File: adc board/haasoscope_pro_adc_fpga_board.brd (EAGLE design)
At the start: 220 x 160 mm, 558 parts, among them CN2 12Vin, IC1 ADC12DL2500ACF, IC13 LMH5401IRMST, IC14 LMH6401IRMZR, IC15 SN74AVC4T774PWR, IC17 DAC8562SDGSR, IC18 TLV9102IPWR, IC2 SN74AVC4T774PWR, IC21 LMH5401IRMST, IC22 TPS7A7200RGTR, IC23 TPS7A7200RGTR, IC24 TPS7A7200RGTR, IC25 TPS72325DBVR, IC26 TPS7A7200RGTR, IC27 TPS7A7200RGTR, IC28 TPS7A7200RGTR, IC29 LMH6401IRMZR, IC3 ADC102S021CIMM_NOPB, IC30 SN74AVC4T774PWR, IC33 TLV9102IPWR, IC4 TLV9102IPWR, IC5 EP4CE30F23C6N, IC6 EPCQ16ASI8N, IC8 FT232HQ, IC9 93LC56B, J10 8pin, J11 8pin, J13 8pin, J14 2x5, J15 test1, J2 test1, J30 2p-2.54, J31 2p-2.54, J32 2p-2.54, J33 2p-2.54, J34 2p-2.54, J35 2p-2.54, J36 2p-2.54, J37 2p-2.54, J39 2p-2.54, J40 2p-2.54, J41 2p-2.54, J42 2p-2.54, J43 2p-2.54, J44 2p-2.54, J45 2p-2.54, J46 2p-2.54, J8 8pin, K10 G6K-2F-RF-DC3, K11 G6K-2F-RF-DC3, K12 G6K-2F-RF-DC3, K5 AQY21SOP, K6 G6K-2F-RF-DC3, K7 G6K-2F-RF-DC3, K9 AQY21SOP, Q4 S8050, Q5 S8050, Q7 S8050, Q8 S8050, Q9 S8050, SW3 SKQGADE010, SW4 SKQGADE010, U2 ADF4350BCPZ, U6 AMS1117-1.2, X1 USBC, Y2 OSCILLATORSMD-5X3, Y3 12MHz

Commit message: minor vias etc
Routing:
- net 2V5-: track 126.2 -> 131.7 mm, vias 22 -> 24
- net 2V5+: track 147.5 -> 152.9 mm, vias 23 -> 25
- net AMPSCLK: track 17.7 -> 22.2 mm
- net AMPSCS: track 17.8 -> 19.7 mm
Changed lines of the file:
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@@
 <wire x1="69.5" y1="41.5" x2="69.9" y2="41.5" width="0.1524" layer="1"/>
 <wire x1="69.9" y1="41.5" x2="70.4" y2="41" width="0.1524" layer="1"/>
-<wire x1="70.4" y1="41" x2="71" y2="41" width="0.1524" layer="1"/>
-<wire x1="71" y1="41" x2="71.2" y2="40.8" width="0.1524" layer="1"/>
+<wire x1="70.4" y1="41" x2="70.56" y2="41" width="0.1524" layer="1"/>
+<wire x1="70.76" y1="40.8" x2="71.2" y2="40.8" width="0.1524" layer="1"/>
+<wire x1="70.76" y1="40.8" x2="70.56" y2="41" width="0.1524" layer="1"/>
 <wire x1="71.2" y1="40.8" x2="72.2390125" y2="40.8" width="0.1524" layer="1"/>
 <wire x1="72.531" y1="40.881" x2="72.65" y2="41" width="0.1524" layer="1"/>
@@
 <wire x1="47.5" y1="115" x2="47.562" y2="115.025" width="0.1524" layer="1"/>
 <wire x1="87" y1="49" x2="86" y2="49" width="0.1524" layer="1"/>
+<via x="70.5" y="103" extent="1-16" drill="0.35"/>
+<wire x1="71.85" y1="102.75" x2="71.49" y2="102.75" width="0.2" layer="1"/>
+<wire x1="71.49" y1="102.75" x2="71.23" y2="103.01" width="0.2" layer="1"/>
+<wire x1="71.23" y1="103.01" x2="70.51" y2="103.01" width="0.2" layer="1"/>
+<wire x1="70.51" y1="103.01" x2="70.5" y2="103" width="0.2" layer="1"/>
+<wire x1="70.5" y1="103" x2="69.546025" y2="103" width="0.2" layer="1"/>
+<wire x1="69.546025" y1="103" x2="69.444025" y2="102.898" width="0.2" layer="1"/>
+<wire x1="69.444025" y1="102.898" x2="69.198" y2="102.898" width="0.2" layer="1"/>
+<wire x1="69.198" y1="102.898" x2="69.05" y2="102.75" width="0.2" layer="1"/>
+<via x="70.78" y="115.7" extent="1-16" drill="0.35"/>
+<wire x1="70.58" y1="115.5" x2="70.78" y2="115.7" width="0.1524" layer="1"/>
+<wire x1="69.35" y1="115.5" x2="70.58" y2="115.5" width="0.1524" layer="1"/>
+<wire x1="71.6" y1="115.5" x2="70.98" y2="115.5" width="0.1524" layer="1"/>
+<wire x1="70.98" y1="115.5" x2="70.78" y2="115.7" width="0.1524" layer="1"/>
 </signal>
 <signal name="2V5-" class="1">
@@
 <wire x1="70.029" y1="52.129" x2="70.15" y2="52.25" width="0.1524" layer="1"/>
 <wire x1="70.15" y1="52.25" x2="70.4657875" y2="52.25" width="0.1524" layer="1"/>
-<wire x1="70.4657875" y1="52.25" x2="70.5697875" y2="52.354" width="0.1524" layer="1"/>
-<wire x1="71.454" y1="52.354" x2="71.5" y2="52.4" width="0.1524" layer="1"/>
-<wire x1="70.5697875" y1="52.354" x2="71.454" y2="52.354" width="0.1524" layer="1"/>
+<wire x1="70.4657875" y1="52.25" x2="70.6197875" y2="52.404" width="0.1524" layer="1"/>
+<wire x1="71.5" y1="52.4" x2="71.496" y2="52.404" width="0.1524" layer="1"/>
+<wire x1="71.496" y1="52.404" x2="70.6197875" y2="52.404" width="0.1524" layer="1"/>
 <wire x1="71.5" y1="52.4" x2="72.5157875" y2="52.4" width="0.1524" layer="1"/>
 <wire x1="72.831" y1="52.369" x2="72.95" y2="52.25" width="0.1524" layer="1"/>
@@
 <wire x1="20.5" y1="123.625" x2="20.5" y2="123.7" width="0.1524" layer="1"/>
 <wire x1="51.5" y1="119" x2="52.95" y2="119" width="0.1524" layer="1"/>
+<via x="70.5" y="104" extent="1-16" drill="0.35"/>
+<wire x1="69.05" y1="104.25" x2="69.38" y2="104.25" width="0.2" layer="1"/>
+<wire x1="69.63" y1="104" x2="70.5" y2="104" width="0.2" layer="1"/>
+<wire x1="69.63" y1="104" x2="69.38" y2="104.25" width="0.2" layer="1"/>
+<wire x1="70.5" y1="104" x2="71.353975" y2="104" width="0.2" layer="1"/>
+<wire x1="71.353975" y1="104" x2="71.455975" y2="104.102" width="0.2" layer="1"/>
+<wire x1="71.455975" y1="104.102" x2="71.702" y2="104.102" width="0.2" layer="1"/>
+<wire x1="71.702" y1="104.102" x2="71.85" y2="104.25" width="0.2" layer="1"/>
+<via x="70.15" y="116.34" extent="1-16" drill="0.35"/>
+<wire x1="69.35" y1="116.5" x2="69.51" y2="116.34" width="0.1524" layer="1"/>
+<wire x1="70.15" y1="116.34" x2="69.51" y2="116.34" width="0.1524" layer="1"/>
+<wire x1="71.65" y1="116.5" x2="71.49" y2="116.34" width="0.1524" layer="1"/>
+<wire x1="71.49" y1="116.34" x2="70.15" y2="116.34" width="0.1524" layer="1"/>
 </signal>
 <signal name="SCS3_IN1">
@@
 <wire x1="85.5" y1="53" x2="85.5" y2="51.087" width="0.1524" layer="1"/>
 <wire x1="85.5" y1="51.087" x2="85.475" y2="51.062" width="0.1524" layer="1"/>
-<wire x1="70.75" y1="53.25" x2="70.15" y2="53.25" width="0.0889" layer="1"/>
-<wire x1="70.875" y1="53.125" x2="70.75" y2="53.25" width="0.0889" layer="1"/>
-<wire x1="71.875" y1="53.125" x2="70.875" y2="53.125" width="0.0889" layer="3"/>
-<wire x1="72.25" y1="53.5" x2="71.875" y2="53.125" width="0.0889" layer="3"/>
-<wire x1="85" y1="53.5" x2="72.25" y2="53.5" width="0.0889" layer="3"/>
+<wire x1="85" y1="53.5" x2="73.5" y2="53.5" width="0.0889" layer="3"/>
 <wire x1="85.5" y1="53" x2="85" y2="53.5" width="0.0889" layer="3"/>
-<via x="70.875" y="53.125" extent="1-16" drill="0.2"/>
+<via x="68" y="53" extent="1-16" drill="0.35"/>
+<wire x1="69.31493125" y1="53.21645" x2="68.94506875" y2="53.21645" width="0.0889" layer="3"/>
+<wire x1="68.94506875" y1="53.21645" x2="68.72861875" y2="53" width="0.0889" layer="3"/>
+<wire x1="68.72861875" y1="53" x2="68" y2="53" width="0.0889" layer="3"/>
+<wire x1="73.5" y1="53.5" x2="73.15355" y2="53.15355" width="0.0889" layer="3"/>
+<wire x1="73.15355" y1="53.15355" x2="69.37783125" y2="53.15355" width="0.0889" layer="3"/>
+<wire x1="69.37783125" y1="53.15355" x2="69.31493125" y2="53.21645" width="0.0889" layer="3"/>
+<wire x1="68" y1="53" x2="68.25" y2="53.25" width="0.0889" layer="1"/>
+<wire x1="68.25" y1="53.25" x2="70.15" y2="53.25" width="0.0889" layer="1"/>
 </signal>
 <signal name="AMPSCS">
@@
 <wire x1="84.875" y1="51" x2="84.825" y2="51.062" width="0.1524" layer="1"/>
 <via x="85.125" y="49.75" extent="1-16" drill="0.3048"/>
-<wire x1="71.125" y1="52.75" x2="70.15" y2="52.75" width="0.0889" layer="1"/>
-<wire x1="71.25" y1="52.875" x2="71.125" y2="52.75" width="0.0889" layer="1"/>
-<wire x1="72.25" y1="52.875" x2="71.25" y2="52.875" width="0.0889" layer="1"/>
-<wire x1="74.875" y1="50.25" x2="72.25" y2="52.875" width="0.0889" layer="3"/>
-<wire x1="84.625" y1="50.25" x2="74.875" y2="50.25" width="0.0889" layer="3"/>
 <wire x1="85.125" y1="49.75" x2="84.625" y2="50.25" width="0.0889" layer="3"/>
-<via x="72.25" y="52.875" extent="1-16" drill="0.2"/>
+<wire x1="71.65" y1="50.25" x2="69.13" y2="52.77" width="0.0889" layer="3"/>
+<via x="69.13" y="52.77" extent="1-16" drill="0.35"/>
+<wire x1="69.13" y1="52.77" x2="70.13" y2="52.77" width="0.0889" layer="1"/>
+<wire x1="70.13" y1="52.77" x2="70.15" y2="52.75" width="0.0889" layer="1"/>
+<wire x1="84.625" y1="50.25" x2="71.65" y2="50.25" width="0.0889" layer="3"/>
 </signal>
 <signal name="AOFFSET">

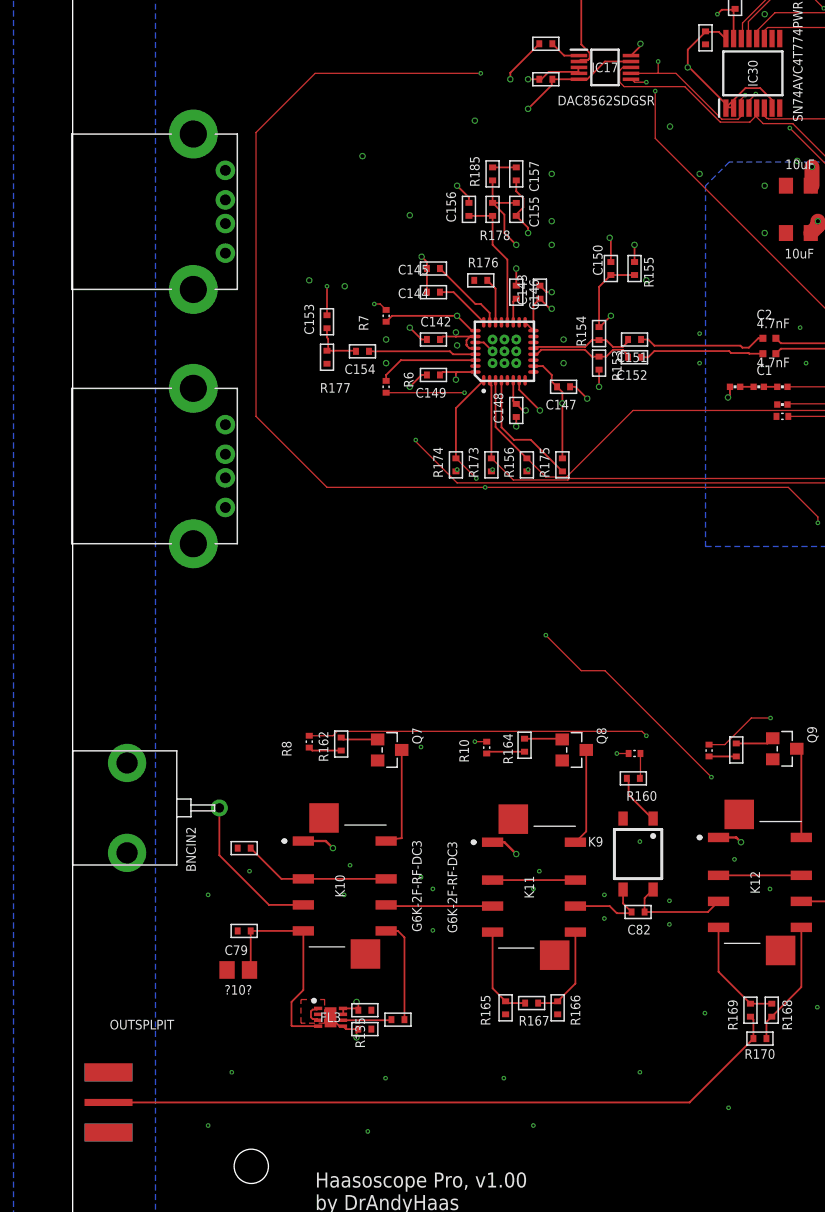
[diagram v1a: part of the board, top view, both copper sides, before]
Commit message: move connectors a little
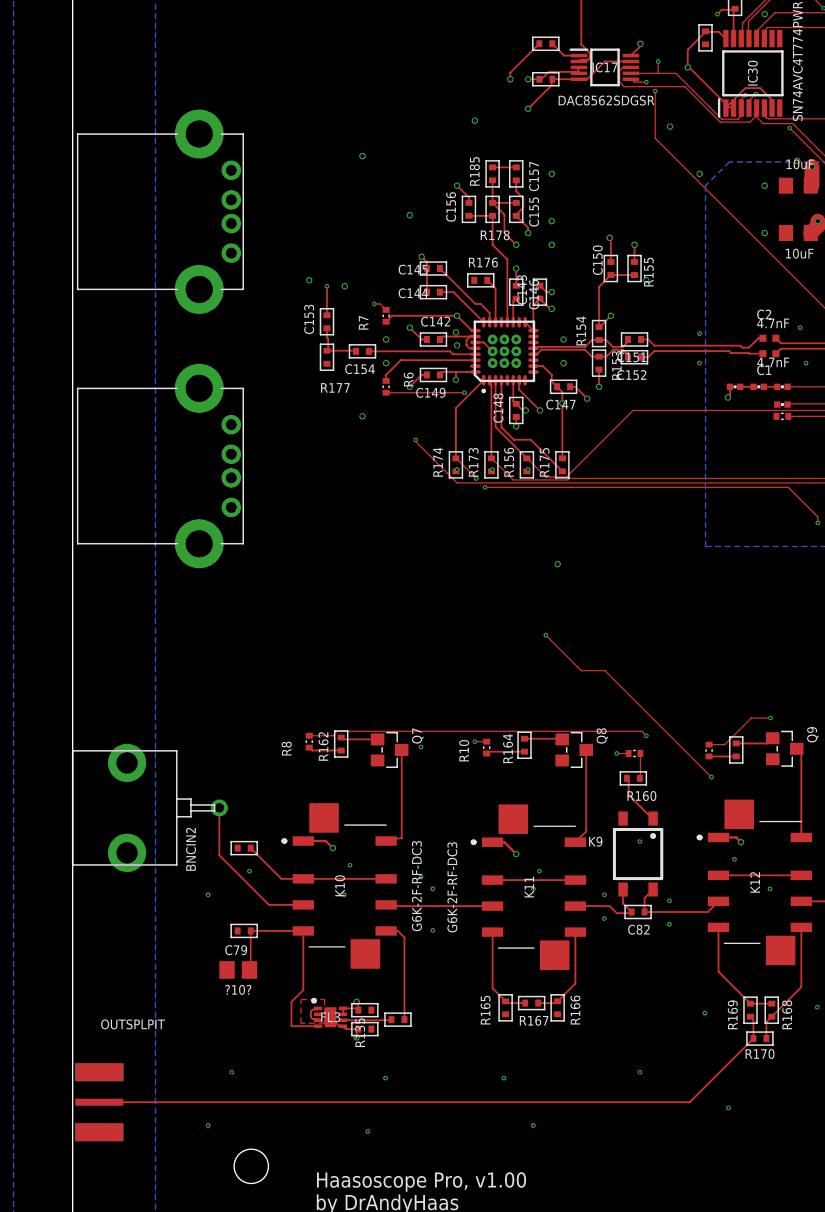
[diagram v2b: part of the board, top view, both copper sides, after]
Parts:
- moved OUTSPLPIT 0.78 mm to (0.22, 15.5)
- moved J15 0.50 mm to (10.7, 69.3)
- moved J2 0.50 mm to (10.7, 90.8)
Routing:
- net SCLK3: track 299.1 -> 291.5 mm, vias 11 -> 10
- net OUTSPLIT: track 58.7 -> 59.5 mm
- net GND: vias 460 -> 462
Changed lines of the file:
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@@
 <drawing>
 <settings>
-<setting alwaysvectorfont="yes"/>
+<setting alwaysvectorfont="no"/>
 <setting verticaltext="up"/>
 </settings>
@@
 </element>
 <element name="U$3" library="FlashPCB_Connectors" package="RJ45_THT_RA_AMPH-FRJAE448" value="RJ45-CONNECTOR-SHIELDED" x="213.6" y="127.2" smashed="yes" rot="R90"/>
-<element name="J15" library="FlashPCB_Connectors" package="USB-2.0-A-THT-RA-TE_AMP-292303-1" value="test1" x="10.2" y="69.3" smashed="yes" rot="R270"/>
+<element name="J15" library="FlashPCB_Connectors" package="USB-2.0-A-THT-RA-TE_AMP-292303-1" value="test1" x="10.7" y="69.3" smashed="yes" rot="R270"/>
 <element name="IC8" library="microbuilder" package="QFN48_8MM" value="FT232HQ" x="148.6645" y="77.4115" smashed="yes" rot="R180"/>
 <element name="IC9" library="microchip" package="SOT23-6" value="93LC56B" x="149.089053125" y="67.43989375" smashed="yes" rot="R180">
@@
 <attribute name="VOLTAGE" value="" x="57.8" y="127.1" size="1.778" layer="27" display="off"/>
 </element>
-<element name="J2" library="FlashPCB_Connectors" package="USB-2.0-A-THT-RA-TE_AMP-292303-1" value="test1" x="10.2" y="90.8" smashed="yes" rot="R270"/>
+<element name="J2" library="FlashPCB_Connectors" package="USB-2.0-A-THT-RA-TE_AMP-292303-1" value="test1" x="10.7" y="90.8" smashed="yes" rot="R270"/>
 <element name="C107" library="MF_Passives" package="C0402" value="0.1uF" x="74.5" y="115" smashed="yes">
 <attribute name="DIELECTRIC" value="" x="74.5" y="115" size="1.778" layer="27" display="off"/>
@@
 <element name="R13" library="FlashPCB_Resistors" package="RES-0402" value="1k" x="57.5" y="140" smashed="yes" rot="R180"/>
 <element name="R22" library="FlashPCB_Resistors" package="RES-0402" value="1k" x="39" y="147" smashed="yes" rot="R90"/>
-<element name="OUTSPLPIT" library="adafruit" package="SMA_EDGELAUNCH" value="50" x="1" y="15.5" smashed="yes">
-<attribute name="NAME" x="8.58" y="22.485" size="0.8128" layer="25" ratio="18" rot="R180"/>
+<element name="OUTSPLPIT" library="adafruit" package="SMA_EDGELAUNCH" value="50" x="0.22" y="15.52" smashed="yes">
+<attribute name="NAME" x="7.8" y="22.505" size="0.8128" layer="25" ratio="18" rot="R180"/>
 </element>
 <element name="R23" library="PP_Passives" package="0201" value="100" x="116.5" y="69.5" smashed="yes" rot="MR270"/>
@@
 <via x="106.45" y="95.05" extent="1-16" drill="0.2"/>
 <via x="112.45" y="95.55" extent="1-16" drill="0.2"/>
+<via x="24.5" y="73.5" extent="1-16" drill="0.35"/>
+<via x="41" y="61" extent="1-16" drill="0.35"/>
 </signal>
 <signal name="3V3" class="1">
@@
 <wire x1="80.5" y1="54.5" x2="80.5" y2="57.25" width="0.0889" layer="1"/>
 <wire x1="34.125" y1="68.25" x2="32.5" y2="69.875" width="0.0889" layer="1"/>
-<wire x1="34.875" y1="67.5" x2="34.125" y2="68.25" width="0.0889" layer="3"/>
+<wire x1="34.875" y1="67.5" x2="34.1875" y2="68.1875" width="0.0889" layer="3"/>
+<wire x1="34.1875" y1="68.1875" x2="34.125" y2="68.25" width="0.0889" layer="3"/>
 <wire x1="34.875" y1="67.5" x2="60.5" y2="67.5" width="0.0889" layer="1"/>
 <wire x1="32.5" y1="69.875" x2="32.4" y2="69.95" width="0.0889" layer="1"/>
@@
 <wire x1="81.5" y1="60" x2="83" y2="60" width="0.0889" layer="1"/>
 <wire x1="83" y1="60" x2="83.125" y2="59.875" width="0.0889" layer="1"/>
-<wire x1="15.5" y1="73.5" x2="15.5" y2="97.5" width="0.0889" layer="1"/>
-<wire x1="15.5" y1="97.5" x2="20.5" y2="102.5" width="0.0889" layer="1"/>
-<via x="34.5" y="102.5" extent="1-16" drill="0.2"/>
-<wire x1="34.5" y1="102.5" x2="35.5" y2="103.5" width="0.0889" layer="3"/>
-<wire x1="35.5" y1="103.5" x2="49.5" y2="103.5" width="0.0889" layer="3"/>
 <via x="49.5" y="103.5" extent="1-16" drill="0.2"/>
 <wire x1="49.5" y1="103.5" x2="49.5" y2="102.5" width="0.0889" layer="1"/>
-<wire x1="34.875" y1="67.5" x2="21.5" y2="67.5" width="0.0889" layer="1"/>
-<wire x1="21.5" y1="67.5" x2="15.5" y2="73.5" width="0.0889" layer="1"/>
-<wire x1="20.5" y1="102.5" x2="34.5" y2="102.5" width="0.0889" layer="1"/>
 <wire x1="73" y1="106.875" x2="72.5" y2="107.375" width="0.0889" layer="3"/>
 <wire x1="72.5" y1="107.375" x2="72.5" y2="107.5" width="0.0889" layer="3"/>
@@
 <wire x1="56.5" y1="100.3047875" x2="56.5" y2="99.5" width="0.0889" layer="1"/>
 <wire x1="71.5" y1="108.5" x2="63" y2="108.5" width="0.0889" layer="3"/>
+<wire x1="28.3125" y1="68.1875" x2="34.1875" y2="68.1875" width="0.0889" layer="3"/>
+<wire x1="49.5" y1="103.5" x2="24.5" y2="103.5" width="0.0889" layer="3"/>
+<wire x1="24.5" y1="103.5" x2="16" y2="95" width="0.0889" layer="3"/>
+<wire x1="16" y1="95" x2="16" y2="80.5" width="0.0889" layer="3"/>
+<wire x1="16" y1="80.5" x2="28.3125" y2="68.1875" width="0.0889" layer="3"/>
 </signal>
 <signal name="SCS3_ADC">
@@
 <wire x1="57.55" y1="20.9" x2="57.55" y2="22.5" width="0.1524" layer="1"/>
 <wire x1="57.55" y1="22.5" x2="57.3" y2="22.75" width="0.1524" layer="1"/>
-<wire x1="57.5" y1="20.85" x2="52.15" y2="15.5" width="0.16" layer="1"/>
-<wire x1="52.15" y1="15.5" x2="3.032" y2="15.5" width="0.16" layer="1"/>
+<wire x1="57.5" y1="20.85" x2="52.17" y2="15.52" width="0.16" layer="1"/>
+<wire x1="52.17" y1="15.52" x2="2.252" y2="15.52" width="0.16" layer="1"/>
 </signal>
 <signal name="OUTMAIN">
